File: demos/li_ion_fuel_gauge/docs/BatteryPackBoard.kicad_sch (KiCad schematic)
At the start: 10 parts, among them J1 Header1xNFemale

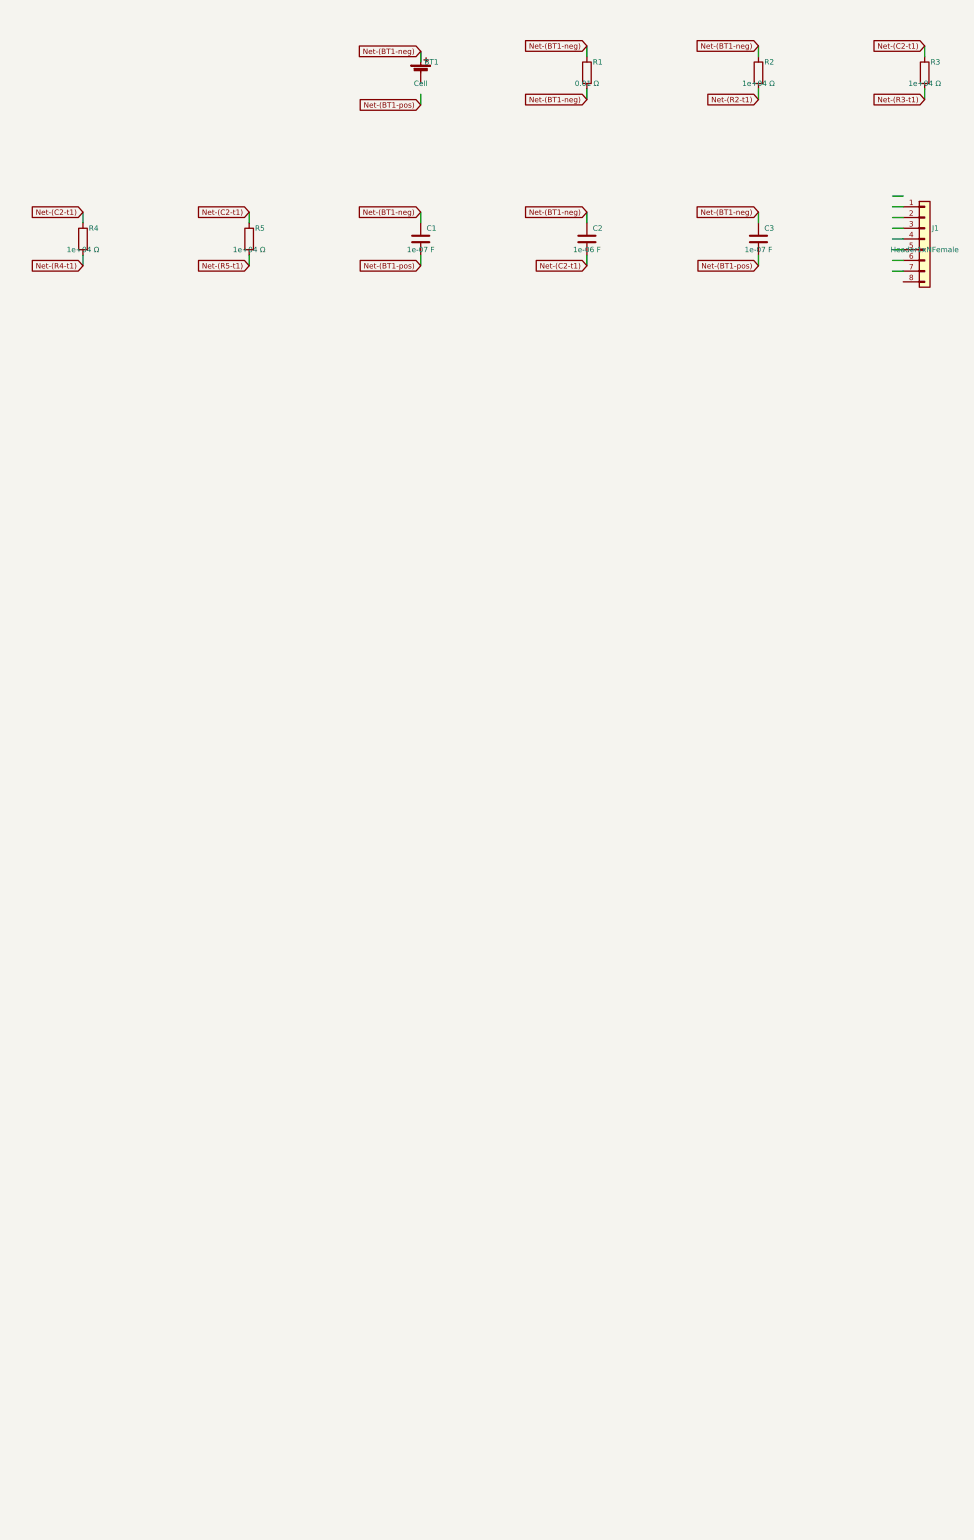
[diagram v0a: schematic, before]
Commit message: export: kicad_sch — Phase 2.5b: layered placement + routing + KiCad 9 fix
Placement (placement.py, complete rewrite):
- Replaces naive grid with Layered Signal Flow algorithm (spec §5 stages 1–8)
- Stage 1: band classification — power chips/rails at top, LEDs at bottom,
  everything else in the signal band
- Stage 2: signal-flow DAG via BFS from Rail/Connector sources; layer = BFS
  distance from nearest source
- Stage 3–4: place within (band, layer) cells at 1500-mil (38.1 mm) same-band
  spacing, 1000-mil inter-band gutter, 25.4 mm page margin
- Stage 6: cluster breakup — up to 10 iterations shifting same-band parts
  that land closer than 0.9× SAME_BAND_SPACING_MM
- Stage 8: page sized to fit (A4 → A3 → A2 → A1)
- grid_place() and sheet_size_mm() kept as shims for backward-compat

Routing (routing.py, new file):
- route_net(): connects stub ends with Manhattan L-shapes (horizontal first)
- find_junctions(): returns points where ≥3 wire endpoints coincide
- renderer uses routed wires between signal-net stub ends

Hierarchical (hierarchical.py, new file):
- collect_boards(), is_multi_board(), sub_sheet_filename() — interface stub
  for multi-Board sub-sheet emission (full implementation deferred)

KiCad 9 sub-symbol name fix (library_loader.py):
- KiCad 9 schematics expect sub-symbols nested inside their parent in
  lib_symbols to use the bare name (R_0_1, LED_0_1, 4069_1_0) — NOT the
  lib-qualified name (Device:R_0_1, Device:LED_0_1, 4xxx:4069_1_0)
- Fixed _qualify_names() to add the lib: prefix only to the exact parent
  symbol name using a lookahead (?=") that prevents sub-unit names from
  being qualified

Tests (+25 tests):
- test_placement.py: band classification, all-on-grid, determinism,
  minimum spacing, power < signal < indicator Y ordering, page sizing
- test_routing.py: H/V segments, L-shapes, orthogonality, grid snap,
  junction detection

Golden files regenerated for all 23 demo designs.
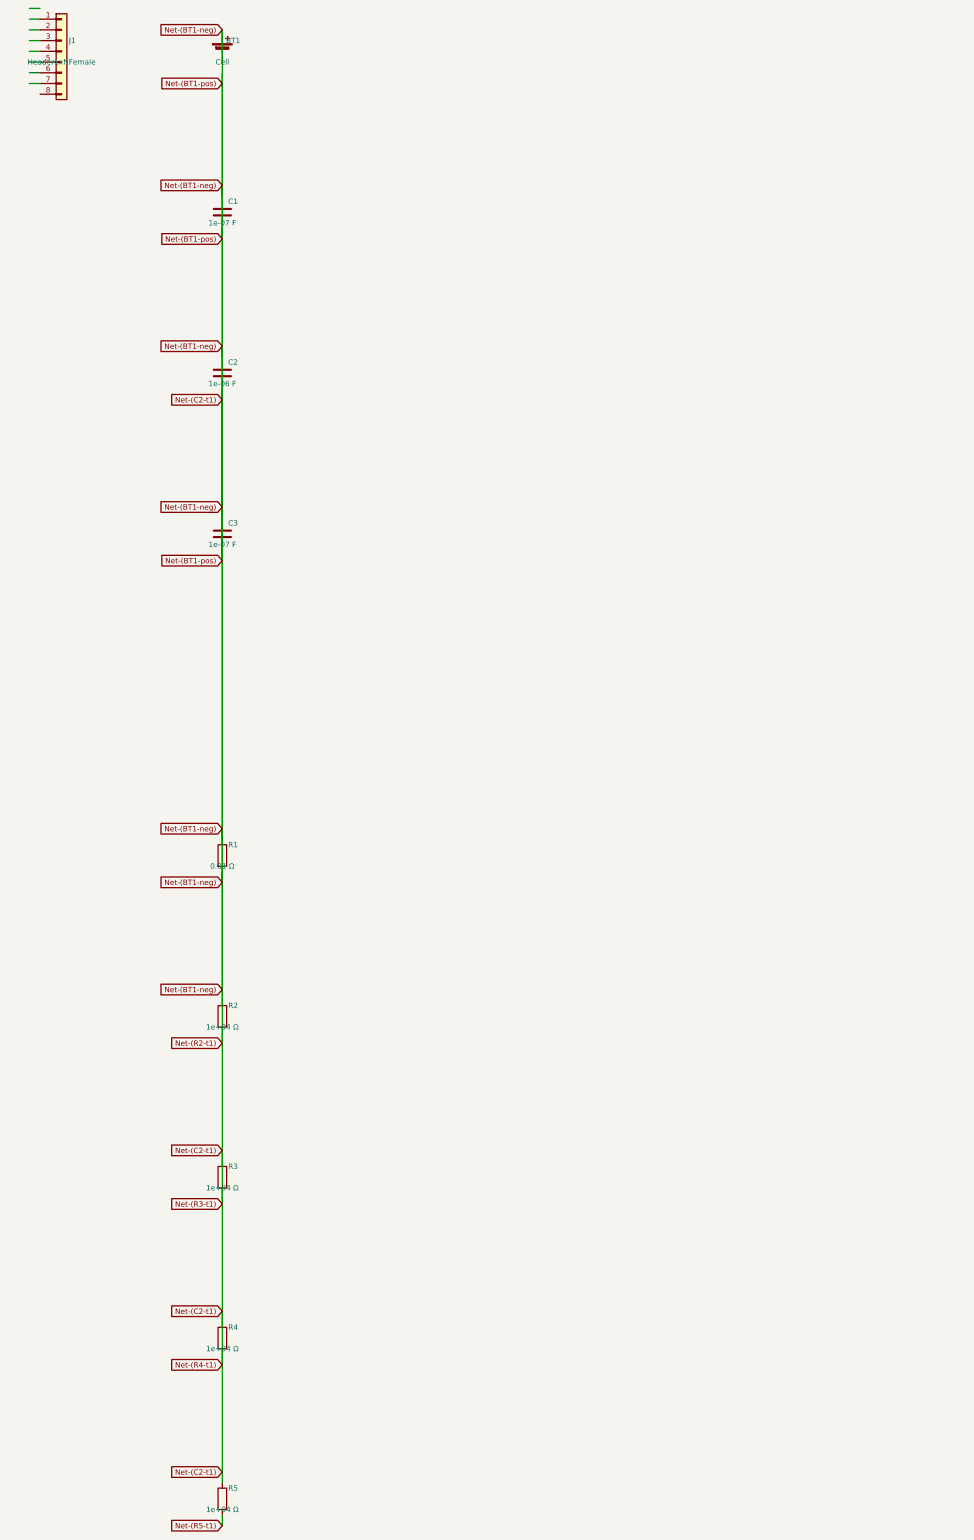
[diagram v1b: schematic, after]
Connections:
- net Net-(BT1-pos) is gone; now on net Net-(BT1-neg): C1.2, C3.2
- net Net-(C2-t1) is gone; now on net Net-(BT1-neg): C2.2, R3.1, R4.1, R5.1
- net Net-(R2-t1) is gone; now on net Net-(BT1-neg): R2.2
- net Net-(R3-t1) is gone; now on net Net-(BT1-neg): R3.2
- net Net-(R4-t1) is gone; now on net Net-(BT1-neg): R4.2
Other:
- moved on the sheet: BT1, C1, C2, C3, J1, R1, R2, R3, R4, R5
